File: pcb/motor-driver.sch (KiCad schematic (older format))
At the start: 16 parts

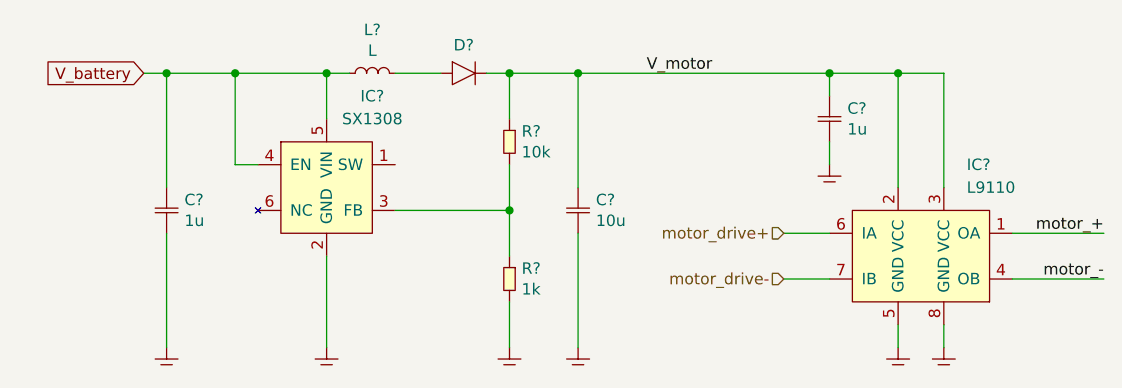
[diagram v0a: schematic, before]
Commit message: added usb interface, switching signal to boost circuits
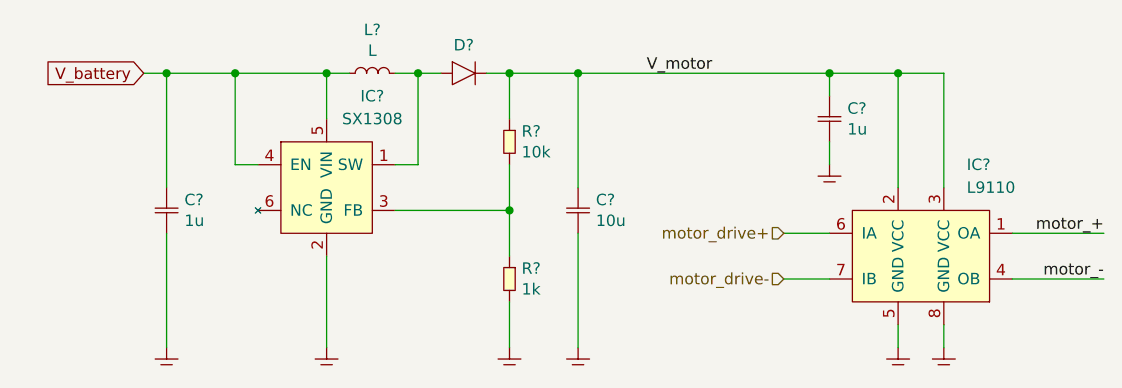
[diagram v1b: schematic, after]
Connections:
- net at IC?.1 (SW): now also D?.1 (A), L?.2
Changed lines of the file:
@@
 $Descr A4 11693 8268
 encoding utf-8
-Sheet 2 4
+Sheet 2 5
 Title ""
 Date ""
@@
 $EndComp
 Wire Wire Line
-	5100 3200 5300 3200
+	5100 3200 5200 3200
 Wire Wire Line
 	4900 3200 4800 3200
@@
 motor_-
 Connection ~ 5900 3200
+Wire Wire Line
+	5100 3600 5200 3600
+Wire Wire Line
+	5200 3600 5200 3200
+Connection ~ 5200 3200
+Wire Wire Line
+	5200 3200 5300 3200
 $EndSCHEMATC
